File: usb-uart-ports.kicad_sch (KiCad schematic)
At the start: 4 parts, among them J7 10129378-902003BLF, J8 10129378-902003BLF

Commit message: first few boards laid out
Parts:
- renumbered C52 to C53, J7 to J25, J8 to J26
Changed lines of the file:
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@@
     (rev "2")
     (company "Oro Operating System")
+    (comment 1 "://oro.sh")
+    (comment 2 "Joshua Lee Junon")
   )
   (junction (at 143.51 91.44) (diameter 0) (color 0 0 0 0)
@@
         )
         (path "/e89dcd22-1250-4a5b-b778-1c95a0dd623d/6f0a294d-fd09-4bb5-9458-a2c8fc68902c"
-          (reference "D12") (unit 1)
+          (reference "D10") (unit 1)
         )
       )
@@
   (symbol (lib_id "SamacSys_Parts:10129378-902003BLF") (at 124.46 104.14 0) (mirror y) (unit 1)
     (in_bom yes) (on_board yes) (dnp no)
-    (property "Reference" "J8" (at 114.3 98.409 0)
+    (property "Reference" "J26" (at 114.3 98.409 0)
       (effects (font (size 1.27 1.27)))
     )
@@
       (project "Oro Link rev2"
         (path "/e89dcd22-1250-4a5b-b778-1c95a0dd623d/6f0a294d-fd09-4bb5-9458-a2c8fc68902c"
-          (reference "J8") (unit 1)
+          (reference "J26") (unit 1)
         )
       )
@@
   (symbol (lib_id "SamacSys_Parts:10129378-902003BLF") (at 124.46 91.44 0) (mirror y) (unit 1)
     (in_bom yes) (on_board yes) (dnp no)
-    (property "Reference" "J7" (at 114.3 85.709 0)
+    (property "Reference" "J25" (at 114.3 85.709 0)
       (effects (font (size 1.27 1.27)))
     )
@@
       (project "Oro Link rev2"
         (path "/e89dcd22-1250-4a5b-b778-1c95a0dd623d/6f0a294d-fd09-4bb5-9458-a2c8fc68902c"
-          (reference "J7") (unit 1)
+          (reference "J25") (unit 1)
         )
       )
@@
   (symbol (lib_id "power:GNDPWR") (at 196.85 109.22 0) (unit 1)
     (in_bom yes) (on_board yes) (dnp no) (fields_autoplaced)
-    (property "Reference" "#PWR099" (at 196.85 114.3 0)
+    (property "Reference" "#PWR0135" (at 196.85 114.3 0)
       (effects (font (size 1.27 1.27)) hide)
     )
@@
       (project "Oro Link rev2"
         (path "/e89dcd22-1250-4a5b-b778-1c95a0dd623d/6f0a294d-fd09-4bb5-9458-a2c8fc68902c"
-          (reference "#PWR099") (unit 1)
+          (reference "#PWR0135") (unit 1)
         )
       )
@@
   (symbol (lib_id "power:GNDPWR") (at 165.1 116.84 0) (unit 1)
     (in_bom yes) (on_board yes) (dnp no) (fields_autoplaced)
-    (property "Reference" "#PWR097" (at 165.1 121.92 0)
+    (property "Reference" "#PWR0133" (at 165.1 121.92 0)
       (effects (font (size 1.27 1.27)) hide)
     )
@@
       (project "Oro Link rev2"
         (path "/e89dcd22-1250-4a5b-b778-1c95a0dd623d/6f0a294d-fd09-4bb5-9458-a2c8fc68902c"
-          (reference "#PWR097") (unit 1)
+          (reference "#PWR0133") (unit 1)
         )
       )
@@
   (symbol (lib_id "SamacSys_Parts:HV2225Y102KXMATHV") (at 168.91 116.84 0) (unit 1)
     (in_bom yes) (on_board yes) (dnp no) (fields_autoplaced)
-    (property "Reference" "C52" (at 175.26 111.3409 0)
+    (property "Reference" "C53" (at 175.26 111.3409 0)
       (effects (font (size 1.27 1.27)))
     )
@@
       (project "Oro Link rev2"
         (path "/e89dcd22-1250-4a5b-b778-1c95a0dd623d/6f0a294d-fd09-4bb5-9458-a2c8fc68902c"
-          (reference "C52") (unit 1)
+          (reference "C53") (unit 1)
         )
       )
@@
   (symbol (lib_id "power:GND") (at 185.42 116.84 0) (unit 1)
     (in_bom yes) (on_board yes) (dnp no) (fields_autoplaced)
-    (property "Reference" "#PWR098" (at 185.42 123.19 0)
+    (property "Reference" "#PWR0134" (at 185.42 123.19 0)
       (effects (font (size 1.27 1.27)) hide)
     )
@@
       (project "Oro Link rev2"
         (path "/e89dcd22-1250-4a5b-b778-1c95a0dd623d/6f0a294d-fd09-4bb5-9458-a2c8fc68902c"
-          (reference "#PWR098") (unit 1)
+          (reference "#PWR0134") (unit 1)
         )
       )
@@
   (symbol (lib_id "power:GNDPWR") (at 153.67 109.22 0) (unit 1)
     (in_bom yes) (on_board yes) (dnp no) (fields_autoplaced)
-    (property "Reference" "#PWR096" (at 153.67 114.3 0)
+    (property "Reference" "#PWR0132" (at 153.67 114.3 0)
       (effects (font (size 1.27 1.27)) hide)
     )
@@
       (project "Oro Link rev2"
         (path "/e89dcd22-1250-4a5b-b778-1c95a0dd623d/6f0a294d-fd09-4bb5-9458-a2c8fc68902c"
-          (reference "#PWR096") (unit 1)
-        )
-      )
+          (reference "#PWR0132") (unit 1)
+        )
+      )

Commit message: first panelization of entire modular dev board
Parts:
- removed C53: 1nF 5kV, CAPC5664X270N, symbol SamacSys_Parts:HV2225Y102KXMATHV
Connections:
- net UART_RX: now also D?.2 (CH2); no longer D?.1 (CH1)
- net UART_TX: now also D?.1 (CH1); no longer D?.2 (CH2)
- net USB_D+: now also D?.5 (CH4); no longer D?.4 (CH3)
- net USB_D-: now also D?.4 (CH3); no longer D?.5 (CH4)
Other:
- moved on the sheet: J25, J26

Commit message: initial board layout
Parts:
- renumbered J25 to J7, J26 to J8
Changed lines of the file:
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@@
         )
         (path "/e89dcd22-1250-4a5b-b778-1c95a0dd623d/6f0a294d-fd09-4bb5-9458-a2c8fc68902c"
-          (reference "D10") (unit 1)
+          (reference "D9") (unit 1)
         )
       )
@@
   (symbol (lib_id "SamacSys_Parts:10129378-902003BLF") (at 124.46 106.68 180) (unit 1)
     (in_bom yes) (on_board yes) (dnp no)
-    (property "Reference" "J26" (at 114.3 98.409 0)
+    (property "Reference" "J8" (at 114.3 98.409 0)
       (effects (font (size 1.27 1.27)))
     )
@@
       (project "Oro Link rev2"
         (path "/e89dcd22-1250-4a5b-b778-1c95a0dd623d/6f0a294d-fd09-4bb5-9458-a2c8fc68902c"
-          (reference "J26") (unit 1)
+          (reference "J8") (unit 1)
         )
       )
@@
   (symbol (lib_id "SamacSys_Parts:10129378-902003BLF") (at 124.46 93.98 180) (unit 1)
     (in_bom yes) (on_board yes) (dnp no)
-    (property "Reference" "J25" (at 114.3 85.709 0)
+    (property "Reference" "J7" (at 114.3 85.709 0)
       (effects (font (size 1.27 1.27)))
     )
@@
       (project "Oro Link rev2"
         (path "/e89dcd22-1250-4a5b-b778-1c95a0dd623d/6f0a294d-fd09-4bb5-9458-a2c8fc68902c"
-          (reference "J25") (unit 1)
+          (reference "J7") (unit 1)
         )
       )
@@
   (symbol (lib_id "power:GNDPWR") (at 196.85 109.22 0) (unit 1)
     (in_bom yes) (on_board yes) (dnp no) (fields_autoplaced)
-    (property "Reference" "#PWR0135" (at 196.85 114.3 0)
+    (property "Reference" "#PWR078" (at 196.85 114.3 0)
       (effects (font (size 1.27 1.27)) hide)
     )
@@
       (project "Oro Link rev2"
         (path "/e89dcd22-1250-4a5b-b778-1c95a0dd623d/6f0a294d-fd09-4bb5-9458-a2c8fc68902c"
-          (reference "#PWR0135") (unit 1)
+          (reference "#PWR078") (unit 1)
         )
       )
@@
   (symbol (lib_id "power:GNDPWR") (at 153.67 109.22 0) (unit 1)
     (in_bom yes) (on_board yes) (dnp no) (fields_autoplaced)
-    (property "Reference" "#PWR0132" (at 153.67 114.3 0)
+    (property "Reference" "#PWR077" (at 153.67 114.3 0)
       (effects (font (size 1.27 1.27)) hide)
     )
@@
       (project "Oro Link rev2"
         (path "/e89dcd22-1250-4a5b-b778-1c95a0dd623d/6f0a294d-fd09-4bb5-9458-a2c8fc68902c"
-          (reference "#PWR0132") (unit 1)
+          (reference "#PWR077") (unit 1)
         )
       )

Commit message: improve ESD, net classes and power diodes
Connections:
- net UART_RX: now also D?.1 (CH1); no longer D?.2 (CH2)
- net UART_TX: now also D?.2 (CH2); no longer D?.1 (CH1)
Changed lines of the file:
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@@
   (junction (at 143.51 91.44) (diameter 0) (color 0 0 0 0)
   )
+  (junction (at 146.05 93.98) (diameter 0) (color 0 0 0 0)
+  )
   (junction (at 143.51 106.68) (diameter 0) (color 0 0 0 0)
-  )
-  (junction (at 146.05 96.52) (diameter 0) (color 0 0 0 0)
   )
   (junction (at 146.05 101.6) (diameter 0) (color 0 0 0 0)
@@
   (no_connect (at 191.77 96.52))
   (no_connect (at 191.77 93.98))
-  (wire (pts (xy 140.97 96.52) (xy 146.05 96.52))
+  (wire (pts (xy 124.46 93.98) (xy 146.05 93.98))
     (stroke (width 0) (type default))
   )
@@
     (stroke (width 0) (type default))
   )
-  (wire (pts (xy 140.97 93.98) (xy 140.97 96.52))
-    (stroke (width 0) (type default))
-  )
   (wire (pts (xy 124.46 106.68) (xy 143.51 106.68))
     (stroke (width 0) (type default))
@@
     (stroke (width 0) (type default))
   )
-  (wire (pts (xy 124.46 93.98) (xy 140.97 93.98))
-    (stroke (width 0) (type default))
-  )
   (wire (pts (xy 146.05 76.2) (xy 137.16 76.2))
     (stroke (width 0) (type default))
@@
     (stroke (width 0) (type default))
   )
-  (wire (pts (xy 143.51 93.98) (xy 143.51 91.44))
+  (wire (pts (xy 143.51 96.52) (xy 143.51 91.44))
     (stroke (width 0) (type default))
   )
@@
     (stroke (width 0) (type default))
   )
+  (wire (pts (xy 146.05 76.2) (xy 146.05 93.98))
+    (stroke (width 0) (type default))
+  )
   (wire (pts (xy 140.97 101.6) (xy 146.05 101.6))
     (stroke (width 0) (type default))
@@
     (stroke (width 0) (type default))
   )
-  (wire (pts (xy 143.51 93.98) (xy 158.75 93.98))
+  (wire (pts (xy 143.51 96.52) (xy 158.75 96.52))
     (stroke (width 0) (type default))
   )
@@
     (stroke (width 0) (type default))
   )
-  (wire (pts (xy 146.05 96.52) (xy 158.75 96.52))
-    (stroke (width 0) (type default))
-  )
-  (wire (pts (xy 146.05 96.52) (xy 146.05 76.2))
+  (wire (pts (xy 146.05 93.98) (xy 158.75 93.98))
     (stroke (width 0) (type default))
   )
@@
         )
         (path "/e89dcd22-1250-4a5b-b778-1c95a0dd623d/6f0a294d-fd09-4bb5-9458-a2c8fc68902c"
-          (reference "D9") (unit 1)
+          (reference "D13") (unit 1)
         )
       )
@@
   (symbol (lib_id "power:GNDPWR") (at 196.85 109.22 0) (unit 1)
     (in_bom yes) (on_board yes) (dnp no) (fields_autoplaced)
-    (property "Reference" "#PWR078" (at 196.85 114.3 0)
+    (property "Reference" "#PWR075" (at 196.85 114.3 0)
       (effects (font (size 1.27 1.27)) hide)
     )
@@
       (project "Oro Link rev2"
         (path "/e89dcd22-1250-4a5b-b778-1c95a0dd623d/6f0a294d-fd09-4bb5-9458-a2c8fc68902c"
-          (reference "#PWR078") (unit 1)
+          (reference "#PWR075") (unit 1)
         )
       )
@@
   (symbol (lib_id "power:GNDPWR") (at 153.67 109.22 0) (unit 1)
     (in_bom yes) (on_board yes) (dnp no) (fields_autoplaced)
-    (property "Reference" "#PWR077" (at 153.67 114.3 0)
+    (property "Reference" "#PWR074" (at 153.67 114.3 0)
       (effects (font (size 1.27 1.27)) hide)
     )
@@
       (project "Oro Link rev2"
         (path "/e89dcd22-1250-4a5b-b778-1c95a0dd623d/6f0a294d-fd09-4bb5-9458-a2c8fc68902c"
-          (reference "#PWR077") (unit 1)
-        )
-      )
+          (reference "#PWR074") (unit 1)
+        )
+      )

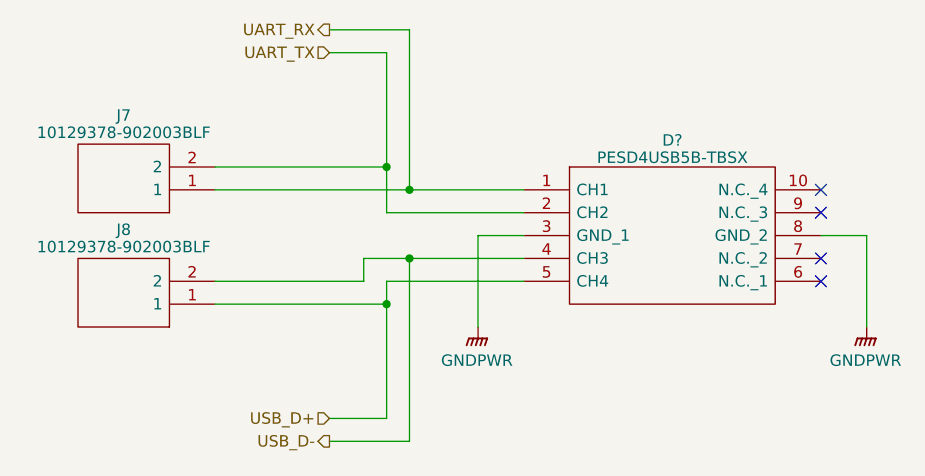
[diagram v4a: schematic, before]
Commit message: initial component layout
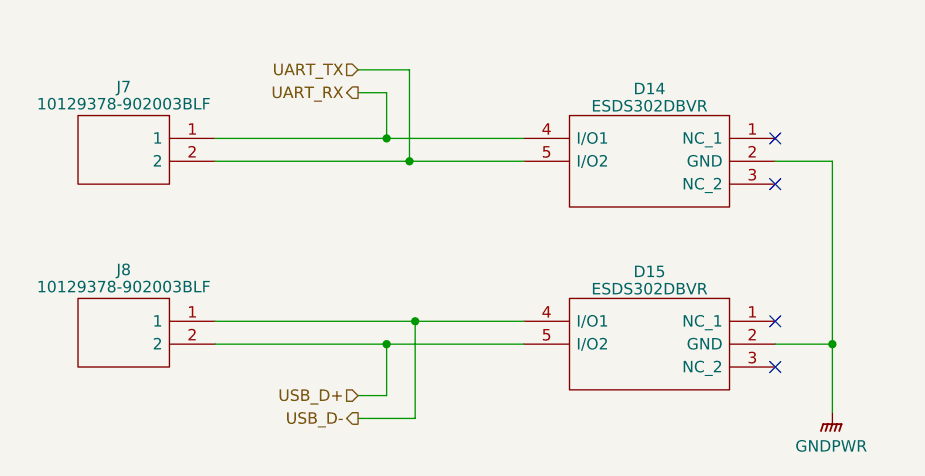
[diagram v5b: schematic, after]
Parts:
- removed D?: PESD4USB5B-TBSX, PESD4USB5BTBSX, symbol SamacSys_Parts:PESD4USB5B-TBSX
- added D14, D15: ESDS302DBVR, SOT95P280X145-5N, symbol SamacSys_Parts:ESDS302DBVR
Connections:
- net GNDPWR: now also D14.2 (GND), D15.2 (GND)
- net UART_RX: now also D14.4 (I/O1)
- net UART_TX: now also D14.5 (I/O2)
- net USB_D+: now also J8.2, D15.5 (I/O2); no longer J8.1
- net USB_D-: now also J8.1, D15.4 (I/O1); no longer J8.2
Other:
- moved on the sheet: J7, J8
